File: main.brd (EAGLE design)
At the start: 50.8 x 50.8 mm, 31 parts

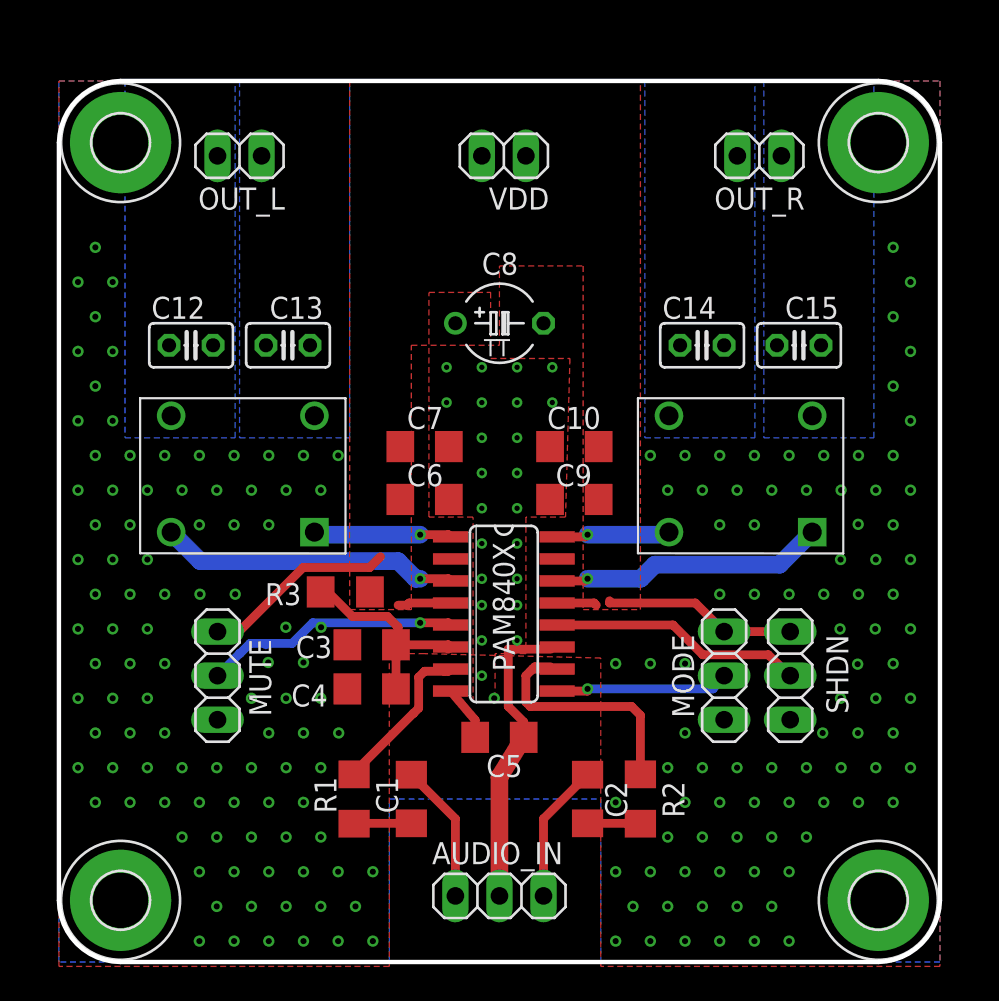
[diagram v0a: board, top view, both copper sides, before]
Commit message: rev 2.0
board size's reduced, main bypass cap's size and value has changed.
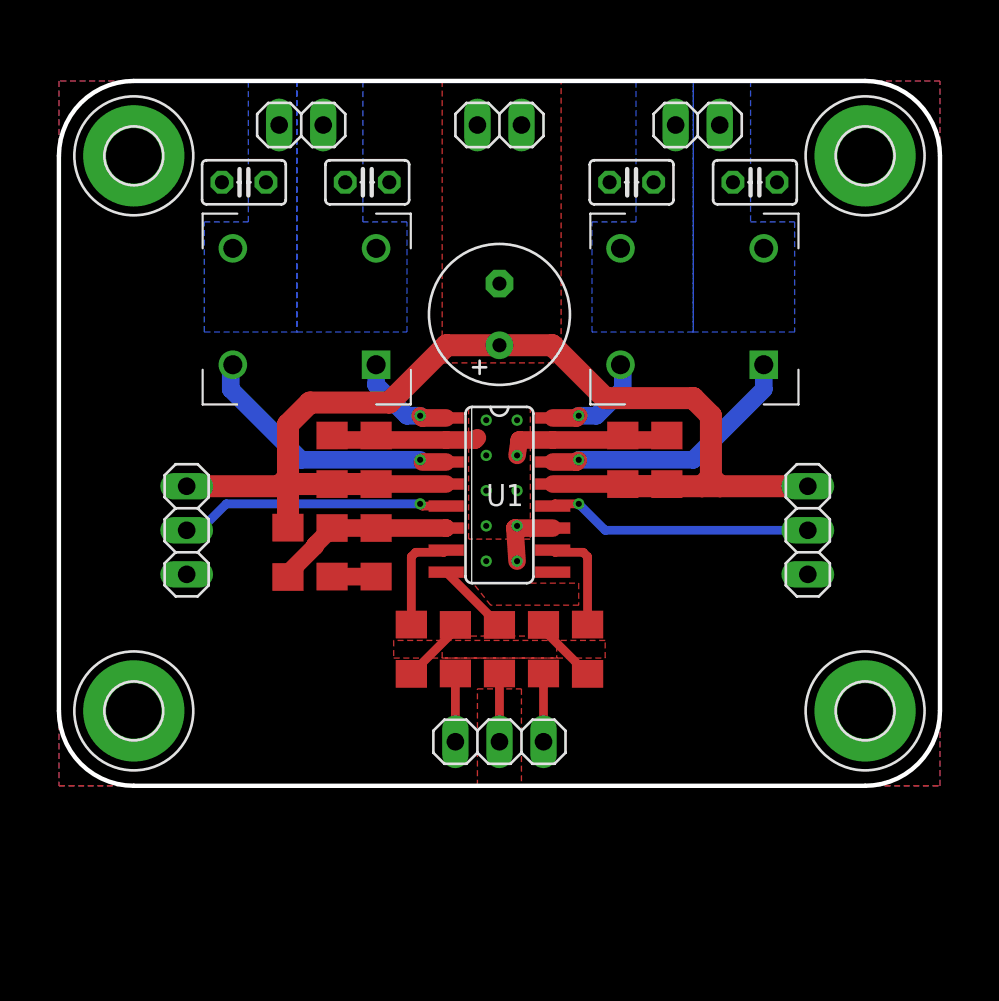
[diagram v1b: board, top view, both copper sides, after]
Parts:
- removed MODE: (no value), pinhead:1X03
- removed PAM840X: (no value), PAM8403:SOP-16
- removed U$1, U$2: JA4575-BL, JA4575-BL:JA4575-BL
- added LEFT_COIL, RIGHT_COIL: JA4575-BL, JA4575-BL:JA4575-BL
- added U1: (no value), PAM8403:SOP-16
- C8: value 1000uF -> (none); device rcl:TAP5-45 -> rcl:E3,5-8
- moved H1 44.3 mm to (46.5, 14.5)
- moved H4 44.3 mm to (4.32, 14.5)
- moved H2 42.9 mm to (46.5, 46.5)
- moved H3 42.9 mm to (4.32, 46.5)
- moved C13 10.5 mm to (17.8, 45.0), turned to 0 degrees
- moved C14 10.2 mm to (33.0, 45.0), turned to 180 degrees
- moved C12 9.88 mm to (10.7, 45.0), turned to 180 degrees
- moved C15 9.74 mm to (40.1, 45.0), turned to 0 degrees
- moved R1 9.25 mm to (20.3, 18.0)
- moved R2 9.16 mm to (30.5, 18.0)
- moved C1 9.00 mm to (22.9, 18.0), turned to 90 degrees
- moved C2 9.00 mm to (27.9, 18.0), turned to 90 degrees
- moved AUDIO_IN 8.89 mm to (25.4, 12.7)
- moved MUTE 8.57 mm to (7.37, 24.9)
- moved SHDN 8.44 mm to (43.2, 24.9)
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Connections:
- removed net D: PAM840X.14, U$2.1
- removed net MODE: MODE.2, PAM840X.9
- new net OUT_R-: RIGHT_COIL.1, U1.14
- net !MUTE: now also U1.5; no longer PAM840X.5
- net !SHND: now also U1.12; no longer PAM840X.12
- net AVDD: now also U1.6; no longer PAM840X.6
- net GND: now also U1.11, U1.15, U1.2, U1.9; no longer MODE.3, PAM840X.11, PAM840X.15, PAM840X.2
- net INL: now also U1.7; no longer PAM840X.7
- net INR: now also U1.10; no longer PAM840X.10
- net N$4: now also LEFT_COIL.4; no longer U$1.4
- net N$6: now also RIGHT_COIL.4; no longer U$2.4
- net N$7: now also RIGHT_COIL.5; no longer U$2.5
- net N$8: now also LEFT_COIL.5; no longer U$1.5
- net OUT_L+: now also LEFT_COIL.1, U1.1; no longer PAM840X.1, U$1.1
- net OUT_L-: now also LEFT_COIL.8, U1.3; no longer PAM840X.3, U$1.8
- net OUT_R+: now also RIGHT_COIL.8, U1.16; no longer PAM840X.16, U$2.8
- net VDD: now also U1.13, U1.4; no longer MODE.1, PAM840X.13, PAM840X.4
- net VREF: now also U1.8; no longer PAM840X.8
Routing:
- net VDD: track 27.8 -> 74.6 mm
- net OUT_R-: track 0.00 -> 16.8 mm, vias 0 -> 1
- net D: track 15.9 -> 0.00 mm, vias 1 -> 0
- net GND: track 17.5 -> 29.2 mm, vias 209 -> 10
- net MODE: track 10.1 -> 0.00 mm, vias 1 -> 0
- net INR: track 14.9 -> 6.08 mm
- net N$5: track 8.04 -> 3.93 mm
- net N$3: track 8.04 -> 3.93 mm
- net INL: track 9.59 -> 6.08 mm
- net OUT_L+: track 7.96 -> 5.99 mm
- net AVDD: track 12.4 -> 10.5 mm
- net OUT_L-: track 17.3 -> 15.6 mm
- net VREF: track 3.19 -> 4.33 mm
- net N$2: track 3.09 -> 3.87 mm
- net !MUTE: track 14.9 -> 15.6 mm
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- added copper zone on layer 1, net N$10
- added copper zone on layer 1, net N$11
- added copper zone on layer 1, net N$12
- added copper zone on layer 1, net N$9
- removed copper zone on layer 16, net N$9
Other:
- board size 50.8 x 50.8 mm -> 50.8 x 40.6 mm
- board text removed: "+"
- board text removed: "FATIH YILMAZ - 2017"
- board text removed: "L"
- board text removed: "LEFT"
- board text removed: "PWR"
- board text removed: "R"
- board text removed: "RIGHT"
- board text removed: "−"

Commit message: New board design
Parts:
- removed AUDIO_IN, MUTE, SHDN: (no value), pinhead:1X03
- removed VDD: (no value), pinhead:1X02
- added C11: (no value), rcl:E3,5-8
- added J1: (no value), SparkFun-Connectors:1X09_NO_SILK
- C12, C13, C14, C15: device rcl:C025-025X050 -> rcl:C050-045X075
- H1, H2, H3, H4: value MOUNT-PAD-ROUND3.2 -> MOUNT-PAD-ROUND3.0; device holes:3,2-PAD -> holes:3,0-PAD
- moved C8 20.4 mm to (43.2, 27.4), turned to 0 degrees
- moved OUT_L 3.78 mm to (16.8, 50.8)
- moved OUT_R 3.78 mm to (34.0, 50.8)
- moved C14 3.18 mm to (30.2, 46.5)
- moved H2 3.18 mm to (48.0, 49.3)
- moved H3 3.18 mm to (2.79, 49.3)
- moved C13 3.18 mm to (20.6, 46.5)
- moved R3 2.79 mm to (13.2, 26.4)
- moved C12 2.75 mm to (13.0, 46.5)
- moved C15 2.75 mm to (37.8, 46.5)
- moved LEFT_COIL 2.59 mm to (20.8, 41.7)
- moved RIGHT_COIL 2.34 mm to (38.4, 41.7)
- moved H1 1.55 mm to (48.0, 14.2)
- moved H4 1.55 mm to (2.79, 14.2)
- moved C10 0.51 mm to (34.5, 29.0)
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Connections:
- removed net !MUTE: MUTE.2, U1.5
- removed net !SHND: SHDN.2, U1.12
- new net MUTE: J1.3, U1.5
- new net SHDN: J1.7, U1.12
- net GND: now also C11.-, H1.B3,0, H2.B3,0, H3.B3,0, H4.B3,0, J1.2, J1.5, J1.8; no longer AUDIO_IN.2, MUTE.3, SHDN.3, VDD.1
- net N$3: now also J1.4; no longer AUDIO_IN.1
- net N$5: now also J1.6; no longer AUDIO_IN.3
- net VDD: now also C11.+, J1.1, J1.9; no longer MUTE.1, SHDN.1, VDD.2
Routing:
- net SHDN: track 0.00 -> 17.2 mm
- net MUTE: track 0.00 -> 15.8 mm, vias 0 -> 1
- net !MUTE: track 15.6 -> 0.00 mm, vias 1 -> 0
- net !SHND: track 15.4 -> 0.00 mm, vias 1 -> 0
- net OUT_L-: track 15.6 -> 13.8 mm
- net OUT_R-: track 16.8 -> 15.6 mm
- net OUT_R+: track 6.20 -> 5.05 mm
- net AVDD: track 10.5 -> 9.42 mm
- net OUT_L+: track 5.99 -> 5.00 mm
- net VDD: track 74.6 -> 73.8 mm
- net GND: track 29.2 -> 28.9 mm, vias 10 -> 161
- added copper zone on layer 1, net N$13
- added copper zone on layer 1, net N$14
- added copper zone on layer 1, net N$15
- added copper zone on layer 1, net N$16
- added copper zone on layer 1, net N$17
- removed copper zone on layer 1, net N$9
- removed copper zone on layer 1, net VDD
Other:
- board size 50.8 x 40.6 mm -> 53.3 x 43.2 mm
- board text added: "COMMON"
- board text added: "GND"
- board text added: "LEFT"
- board text added: "LEFT+"
- board text added: "LEFT−"
- board text added: "MUTE"
- board text added: "RIGHT"
- board text added: "RIGHT+"
- board text added: "RIGHT−"
- board text added: "SHDN"
- board text added: "VCC"
- board text added: "© 2017 FATIH YILMAZ LICENSED UNDER THE TAPR OHL V 1.0"
